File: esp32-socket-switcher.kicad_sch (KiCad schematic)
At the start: 19 parts, among them J1 USB4110GFA, K1 G5CA-1A DC5, Q3 CSD17575Q3T

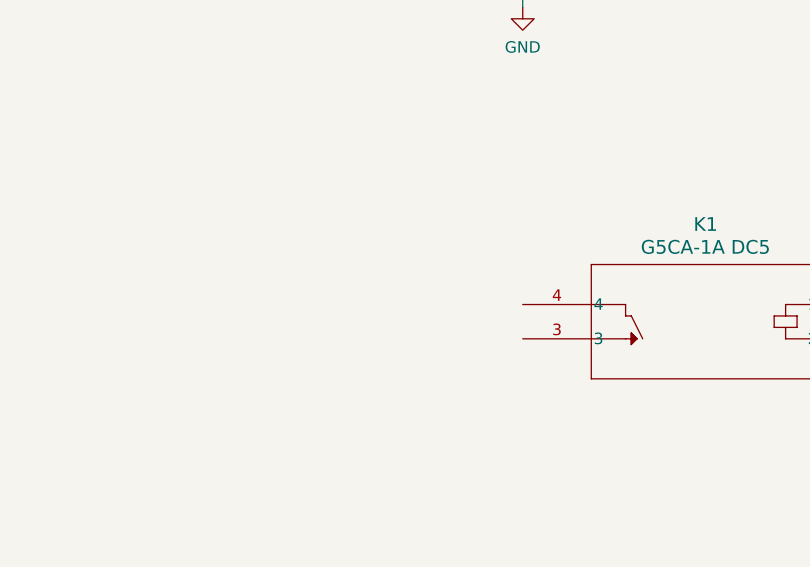
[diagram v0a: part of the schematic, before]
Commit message: mains to relay lable
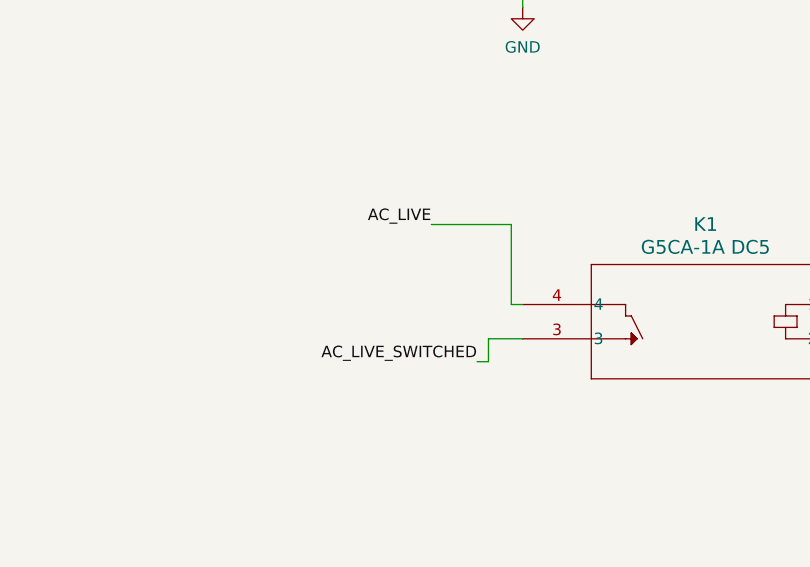
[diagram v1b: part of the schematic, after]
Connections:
- net AC_LIVE: now also K1.4
- net AC_LIVE_SWITCHED: now reaches K1.3
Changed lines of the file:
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@@
+    (stroke (width 0) (type default))
+  )
+  (wire (pts (xy 88.9 95.25) (xy 88.9 92.71))
     (stroke (width 0) (type default))
   )
@@
     (stroke (width 0) (type default))
   )
+  (wire (pts (xy 91.44 88.9) (xy 92.71 88.9))
+    (stroke (width 0) (type default))
+  )
   (wire (pts (xy 33.02 155.575) (xy 35.56 155.575))
     (stroke (width 0) (type default))
   )
+  (wire (pts (xy 91.44 80.01) (xy 91.44 88.9))
+    (stroke (width 0) (type default))
+  )
   (wire (pts (xy 23.495 191.135) (xy 28.575 191.135))
     (stroke (width 0) (type default))
@@
     (stroke (width 0) (type default))
   )
+  (wire (pts (xy 87.63 95.25) (xy 88.9 95.25))
+    (stroke (width 0) (type default))
+  )
   (wire (pts (xy 137.795 180.34) (xy 137.795 173.355))
     (stroke (width 0) (type default))
@@
     (stroke (width 0) (type default))
   )
+  (wire (pts (xy 82.55 80.01) (xy 91.44 80.01))
+    (stroke (width 0) (type default))
+  )
   (wire (pts (xy 92.71 45.72) (xy 92.71 44.45))
     (stroke (width 0) (type default))
@@
     (stroke (width 0) (type default))
   )
+  (wire (pts (xy 88.9 92.71) (xy 92.71 92.71))
+    (stroke (width 0) (type default))
+  )
   (wire (pts (xy 68.58 54.61) (xy 92.71 54.61))
     (stroke (width 0) (type default))
@@
     (effects (font (size 1.27 1.27)) (justify right bottom))
   )
+  (label "AC_LIVE" (at 82.55 80.01 180) (fields_autoplaced)
+    (effects (font (size 1.27 1.27)) (justify right bottom))
+  )
   (label "3V3" (at 156.845 173.355 0) (fields_autoplaced)
     (effects (font (size 1.27 1.27)) (justify left bottom))
@@
     (effects (font (size 1.27 1.27)) (justify left bottom))
   )
+  (label "AC_LIVE_SWITCHED" (at 87.63 95.25 180) (fields_autoplaced)
+    (effects (font (size 1.27 1.27)) (justify right bottom))
+  )
   (label "D-" (at 227.33 111.76 0) (fields_autoplaced)

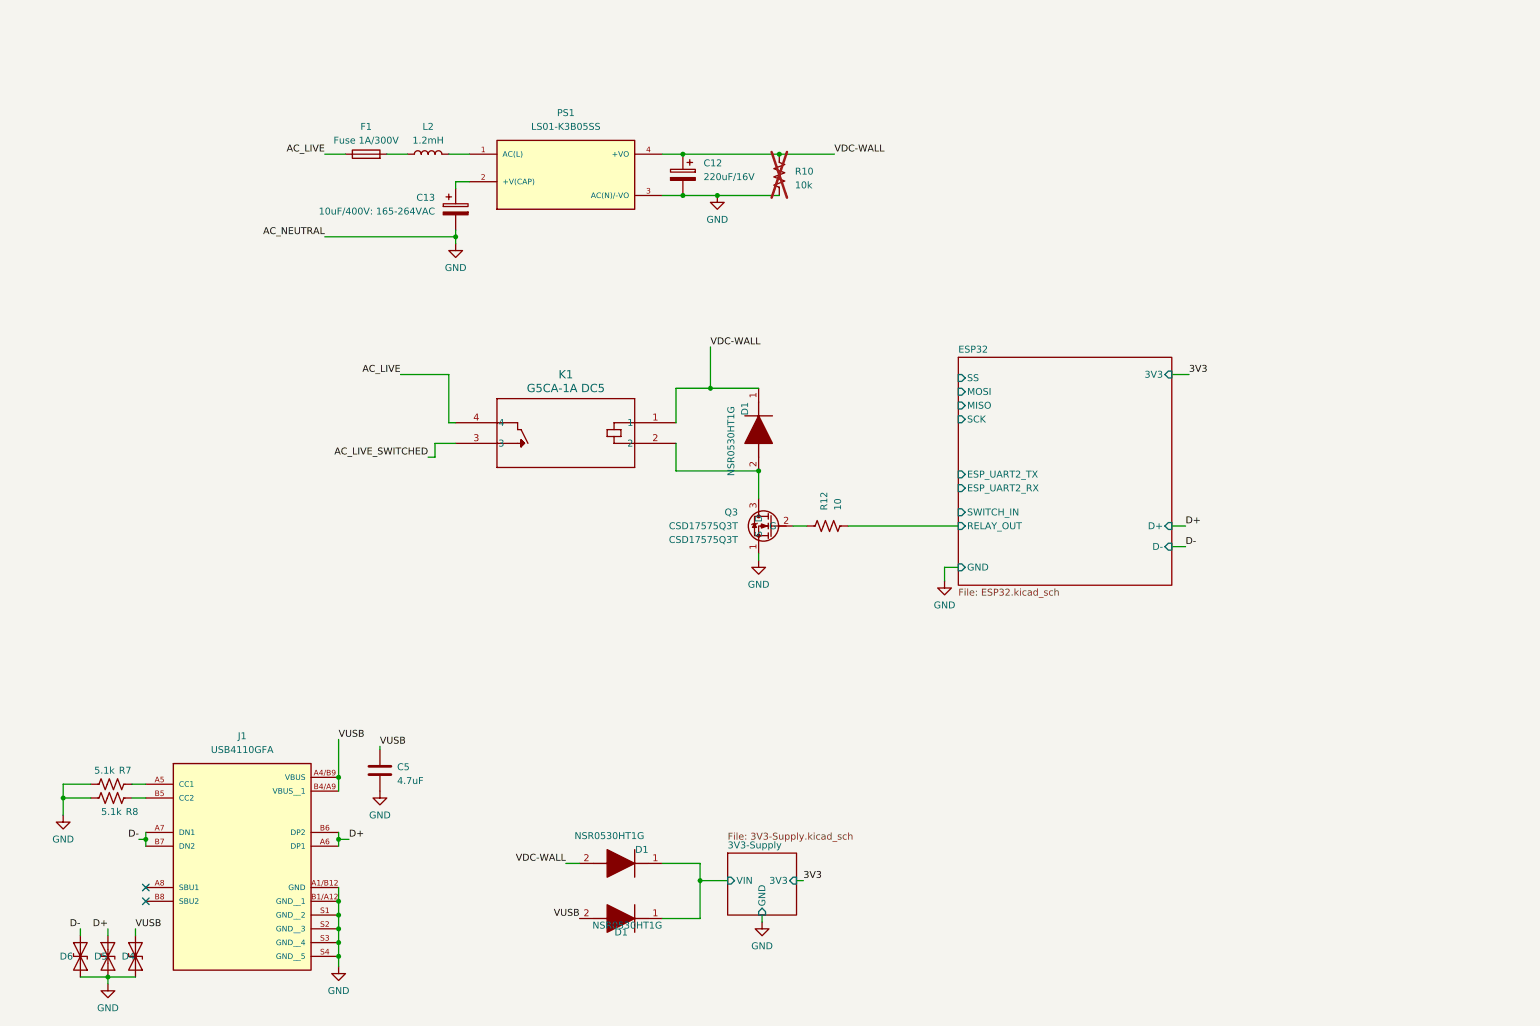
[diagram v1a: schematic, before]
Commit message: added symbols for screw terminals
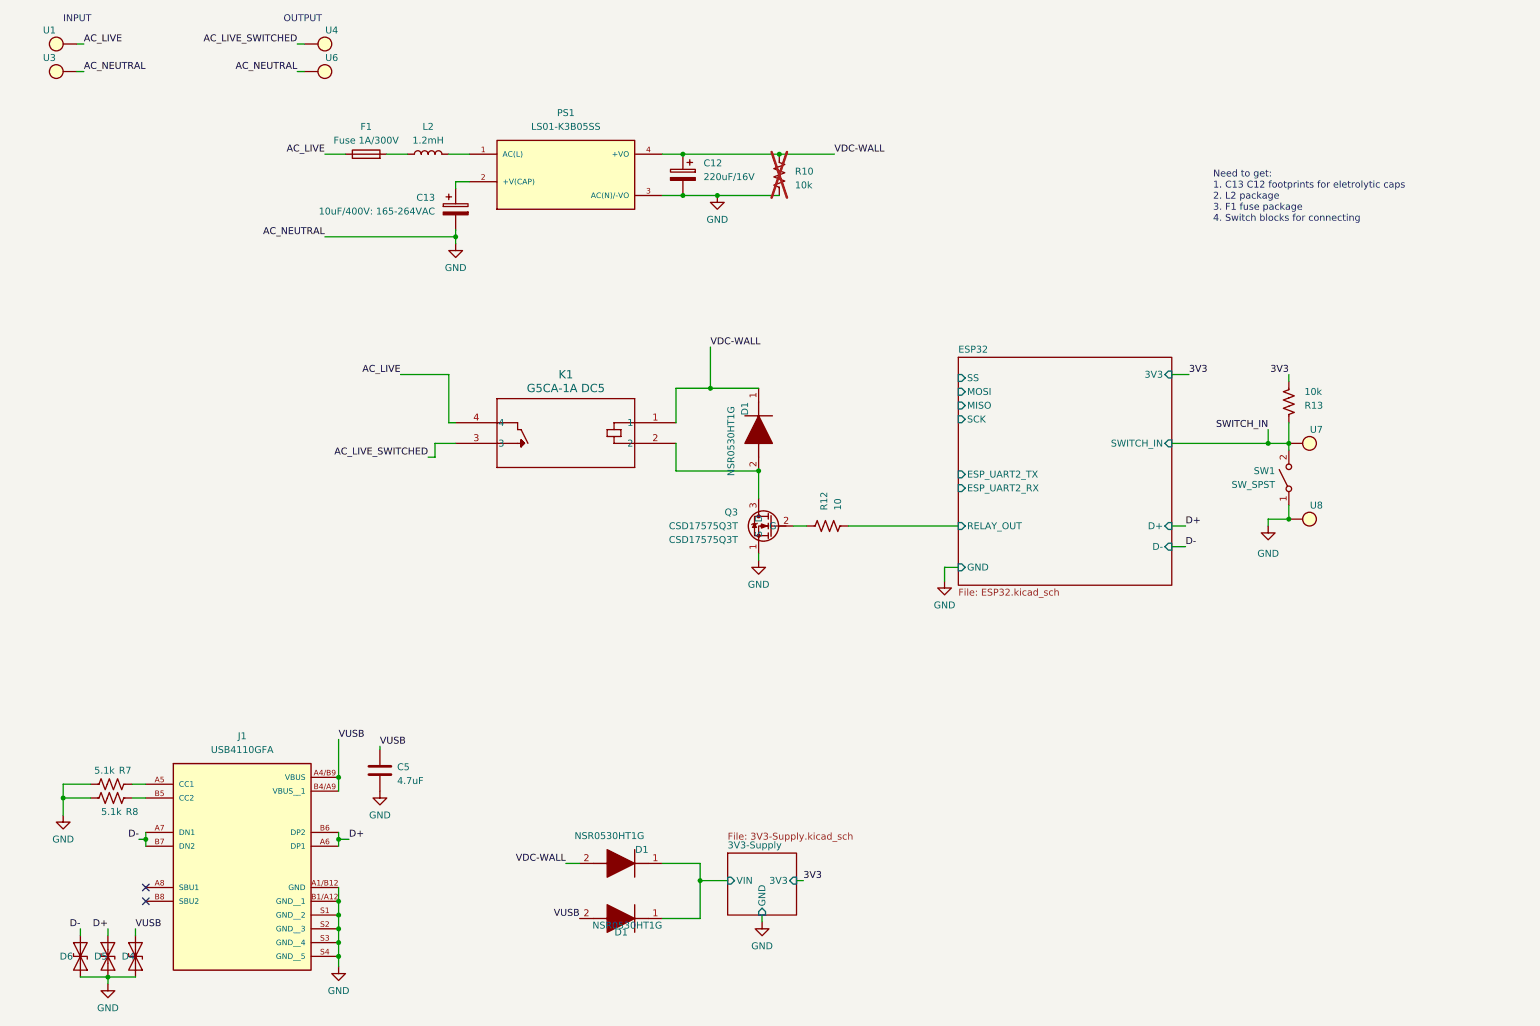
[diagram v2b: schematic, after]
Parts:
- added R13: 10k, esp32-socket-switcher:R_0402_1005Metric, symbol esp32-socket-switcher:Resistor
- added SW1: SW_SPST, symbol Switch:SW_SPST
- added U1, U3, U4, U6, U7, U8: ~, symbol esp32-socket-switcher:PAD_SINGLE
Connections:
- net 3V3: now also R13.1
- net AC_LIVE: now also U1.
- net AC_LIVE_SWITCHED: now also U4.
- net GND: now also SW1.1 (A), U3., U6., U8.
- new net SWITCH_IN: R13.2, SW1.2 (B), U7.
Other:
- note added: "INPUT"
- note added: "Need to get: 1. C13 C12 footprints for eletrolytic caps 2. L2 package 3. F1 fuse package 4. Switch blocks for connecting"
- note added: "OUTPUT"

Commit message: added screw terms. think i need a barrier block instead...
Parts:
- U1, U3, U4, U6, U7, U8: footprint (none) -> esp32-socket-switcher:KEYSTONE_7770
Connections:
- net AC_LIVE: now also U1.1; no longer U1.
- net AC_LIVE_SWITCHED: now also U4.1; no longer U4.
- net GND: now also U3.1, U6.1, U8.1; no longer U3., U6., U8.
- net SWITCH_IN: now also U7.1; no longer U7.
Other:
- note added: "Need to get: 1. C13 C12 footprints for eletrolytic caps 2. L2 package 3. F1 fuse package 4. Replace screw terminals with barrier block(s)"
- note removed: "Need to get: 1. C13 C12 footprints for eletrolytic caps 2. L2 package 3. F1 fuse package 4. Switch blocks for connecting"
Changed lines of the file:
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@@
     (effects (font (size 1.27 1.27)) (justify left bottom))
   )
-  (text "Need to get:\n1. C13 C12 footprints for eletrolytic caps\n2. L2 package\n3. F1 fuse package\n4. Switch blocks for connecting"
+  (text "Need to get:\n1. C13 C12 footprints for eletrolytic caps\n2. L2 package\n3. F1 fuse package\n4. Replace screw terminals with barrier block(s)"
     (at 232.41 52.07 0)
     (effects (font (size 1.27 1.27)) (justify left bottom))
@@
       (effects (font (size 1.27 1.27)))
     )
-    (property "Footprint" "" (at 67.31 19.05 0)
+    (property "Footprint" "esp32-socket-switcher:KEYSTONE_7770" (at 67.31 19.05 0)
       (effects (font (size 1.27 1.27)) hide)
     )
@@
       (effects (font (size 1.27 1.27)) hide)
     )
-    (pin "")
+    (pin "1")
     (instances
       (project "esp32-socket-switcher"
@@
       (effects (font (size 1.27 1.27)))
     )
-    (property "Footprint" "" (at 20.32 19.05 0)
+    (property "Footprint" "esp32-socket-switcher:KEYSTONE_7770" (at 20.32 19.05 0)
       (effects (font (size 1.27 1.27)) hide)
     )
@@
       (effects (font (size 1.27 1.27)) hide)
     )
-    (pin "")
+    (pin "1")
     (instances
       (project "esp32-socket-switcher"
@@
       (effects (font (size 1.27 1.27)))
     )
-    (property "Footprint" "" (at 20.32 24.13 0)
+    (property "Footprint" "esp32-socket-switcher:KEYSTONE_7770" (at 20.32 24.13 0)
       (effects (font (size 1.27 1.27)) hide)
     )
@@
       (effects (font (size 1.27 1.27)) hide)
     )
-    (pin "")
+    (pin "1")
     (instances
       (project "esp32-socket-switcher"
@@
       (effects (font (size 1.27 1.27)))
     )
-    (property "Footprint" "" (at 248.92 92.71 0)
+    (property "Footprint" "esp32-socket-switcher:KEYSTONE_7770" (at 248.92 92.71 0)
       (effects (font (size 1.27 1.27)) hide)
     )
@@
       (effects (font (size 1.27 1.27)) hide)
     )
-    (pin "")
+    (pin "1")
     (instances
       (project "esp32-socket-switcher"
@@
       (effects (font (size 1.27 1.27)))
     )
-    (property "Footprint" "" (at 248.92 106.68 0)
+    (property "Footprint" "esp32-socket-switcher:KEYSTONE_7770" (at 248.92 106.68 0)
       (effects (font (size 1.27 1.27)) hide)
     )
@@
       (effects (font (size 1.27 1.27)) hide)
     )
-    (pin "")
+    (pin "1")
     (instances
       (project "esp32-socket-switcher"
@@
       (effects (font (size 1.27 1.27)))
     )
-    (property "Footprint" "" (at 67.31 24.13 0)
+    (property "Footprint" "esp32-socket-switcher:KEYSTONE_7770" (at 67.31 24.13 0)
       (effects (font (size 1.27 1.27)) hide)
     )
@@
       (effects (font (size 1.27 1.27)) hide)
     )
-    (pin "")
-    (instances
-      (project "esp32-socket-switcher"
+    (pin "1")
+    (instances
+      (project "esp32-socket-switcher"

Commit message: swtiched to barrier block
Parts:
- added J2: 4DB-P108-06, esp32-socket-switcher:TE_2-1437667-9, symbol esp32-socket-switcher:4DB-P108-06
- U1, U3, U4, U6, U7, U8: now left out of the parts list
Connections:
- net AC_LIVE: now also U1., J2.5; no longer U1.1
- net AC_LIVE_SWITCHED: now also U4., J2.6; no longer U4.1
- net GND: now also U3., U6., U8., J2.1, J2.2, J2.3; no longer U3.1, U6.1, U8.1
- net SWITCH_IN: now also U7., J2.4; no longer U7.1
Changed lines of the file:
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@@
   (junction (at 134.62 46.99) (diameter 0) (color 0 0 0 0)
   )
+  (junction (at 34.29 50.8) (diameter 0) (color 0 0 0 0)
+  )
   (junction (at 148.59 97.79) (diameter 0) (color 0 0 0 0)
   )
@@
   )
   (junction (at 140.97 46.99) (diameter 0) (color 0 0 0 0)
+  )
+  (junction (at 34.29 48.26) (diameter 0) (color 0 0 0 0)
   )
   (junction (at 20.32 158.115) (diameter 0) (color 0 0 0 0)
@@
     (stroke (width 0) (type default))
   )
+  (wire (pts (xy 34.29 45.72) (xy 34.29 48.26))
+    (stroke (width 0) (type default))
+  )
   (wire (pts (xy 71.12 179.705) (xy 71.12 177.165))
     (stroke (width 0) (type default))
@@
     (stroke (width 0) (type default))
   )
+  (wire (pts (xy 34.29 48.26) (xy 34.29 50.8))
+    (stroke (width 0) (type default))
+  )
+  (wire (pts (xy 31.75 43.18) (xy 34.29 43.18))
+    (stroke (width 0) (type default))
+  )
   (wire (pts (xy 71.12 184.785) (xy 71.12 182.245))
     (stroke (width 0) (type default))
@@
     (stroke (width 0) (type default))
   )
+  (wire (pts (xy 31.75 40.64) (xy 34.29 40.64))
+    (stroke (width 0) (type default))
+  )
   (wire (pts (xy 63.5 19.05) (xy 64.77 19.05))
     (stroke (width 0) (type default))
@@
   )
   (wire (pts (xy 82.55 80.01) (xy 91.44 80.01))
+    (stroke (width 0) (type default))
+  )
+  (wire (pts (xy 34.29 50.8) (xy 34.29 53.34))
+    (stroke (width 0) (type default))
+  )
+  (wire (pts (xy 31.75 38.1) (xy 34.29 38.1))
     (stroke (width 0) (type default))
   )
@@
     (effects (font (size 1.27 1.27)) (justify right bottom))
   )
+  (label "SWITCH_IN" (at 31.75 43.18 180) (fields_autoplaced)
+    (effects (font (size 1.27 1.27)) (justify right bottom))
+  )
   (label "D+" (at 73.025 165.735 0) (fields_autoplaced)
     (effects (font (size 1.27 1.27)) (justify left bottom))
@@
     (effects (font (size 1.27 1.27)) (justify left bottom))
   )
+  (label "AC_LIVE_SWITCHED" (at 31.75 38.1 180) (fields_autoplaced)
+    (effects (font (size 1.27 1.27)) (justify right bottom))
+  )
   (label "AC_NEUTRAL" (at 63.5 24.13 180) (fields_autoplaced)
     (effects (font (size 1.27 1.27)) (justify right bottom))
@@
   )
   (label "VDC-WALL" (at 113.03 170.18 180) (fields_autoplaced)
+    (effects (font (size 1.27 1.27)) (justify right bottom))
+  )
+  (label "AC_LIVE" (at 31.75 40.64 180) (fields_autoplaced)
     (effects (font (size 1.27 1.27)) (justify right bottom))
   )
@@
   )
   (label "AC_LIVE_SWITCHED" (at 87.63 95.25 180) (fields_autoplaced)
+    (effects (font (size 1.27 1.27)) (justify right bottom))
+  )
+  (label "AC_NEUTRAL" (at 34.29 53.34 180) (fields_autoplaced)
     (effects (font (size 1.27 1.27)) (justify right bottom))
   )
@@
     )
   )
+  (symbol (lib_id "esp32-socket-switcher:4DB-P108-06") (at 44.45 43.18 0) (mirror x) (unit 1)
+    (in_bom yes) (on_board yes) (dnp no)
+    (property "Reference" "J2" (at 50.8 45.72 0)
+      (effects (font (size 1.27 1.27)) (justify left))
+    )
+    (property "Value" "4DB-P108-06" (at 50.8 43.18 0)
+      (effects (font (size 1.27 1.27)) (justify left))
+    )
+    (property "Footprint" "esp32-socket-switcher:TE_2-1437667-9" (at 44.45 43.18 0)
+      (effects (font (size 1.27 1.27)) (justify bottom) hide)
+    )
+    (property "Datasheet" "" (at 44.45 43.18 0)
+      (effects (font (size 1.27 1.27)) hide)
+    )
+    (property "PARTREV" "R" (at 44.45 43.18 0)
+      (effects (font (size 1.27 1.27)) (justify bottom) hide)
+    )
+    (property "STANDARD" "Manufacturer Recommendations" (at 44.45 43.18 0)
+      (effects (font (size 1.27 1.27)) (justify bottom) hide)
+    )
+    (property "MANUFACTURER" "TE" (at 44.45 43.18 0)
+      (effects (font (size 1.27 1.27)) (justify bottom) hide)
+    )
+    (pin "1")
+    (pin "2")
+    (pin "3")
+    (pin "4")
+    (pin "5")
+    (pin "6")
+    (instances
+      (project "esp32-socket-switcher"
+        (path "/19e4cb9f-d0a4-4ce0-8aa4-5fe95563dc37"
+          (reference "J2") (unit 1)
+        )
+      )
+    )
+  )
   (symbol (lib_id "esp32-socket-switcher:PAD_SINGLE") (at 67.31 19.05 0) (mirror y) (unit 1)
-    (in_bom yes) (on_board yes) (dnp no)
+    (in_bom no) (on_board no) (dnp no)
     (property "Reference" "U4" (at 69.85 16.51 0)
       (effects (font (size 1.27 1.27)))
@@
       (effects (font (size 1.27 1.27)) hide)
     )
-    (pin "1")
+    (pin "")
     (instances
       (project "esp32-socket-switcher"
@@
   )
   (symbol (lib_id "esp32-socket-switcher:PAD_SINGLE") (at 20.32 19.05 0) (unit 1)
-    (in_bom yes) (on_board yes) (dnp no)
+    (in_bom no) (on_board no) (dnp no)
     (property "Reference" "U1" (at 17.78 16.51 0)
       (effects (font (size 1.27 1.27)))
@@
       (effects (font (size 1.27 1.27)) hide)
     )
-    (pin "1")
+    (pin "")
     (instances
       (project "esp32-socket-switcher"
@@
   )
   (symbol (lib_id "esp32-socket-switcher:PAD_SINGLE") (at 20.32 24.13 0) (unit 1)
-    (in_bom yes) (on_board yes) (dnp no)
+    (in_bom no) (on_board no) (dnp no)
     (property "Reference" "U3" (at 17.78 21.59 0)
       (effects (font (size 1.27 1.27)))
@@
       (effects (font (size 1.27 1.27)) hide)
     )
-    (pin "1")
+    (pin "")
     (instances
       (project "esp32-socket-switcher"
@@
   )
   (symbol (lib_id "esp32-socket-switcher:PAD_SINGLE") (at 248.92 92.71 0) (mirror y) (unit 1)
-    (in_bom yes) (on_board yes) (dnp no)
+    (in_bom no) (on_board no) (dnp no)
     (property "Reference" "U7" (at 251.46 90.17 0)
       (effects (font (size 1.27 1.27)))
@@
       (effects (font (size 1.27 1.27)) hide)
     )
-    (pin "1")
+    (pin "")
     (instances
       (project "esp32-socket-switcher"
@@
   )
   (symbol (lib_id "esp32-socket-switcher:PAD_SINGLE") (at 248.92 106.68 0) (mirror y) (unit 1)
-    (in_bom yes) (on_board yes) (dnp no)
+    (in_bom no) (on_board no) (dnp no)
     (property "Reference" "U8" (at 251.46 104.14 0)
       (effects (font (size 1.27 1.27)))
@@
       (effects (font (size 1.27 1.27)) hide)
     )
-    (pin "1")
+    (pin "")
     (instances
       (project "esp32-socket-switcher"
@@
   )
   (symbol (lib_id "esp32-socket-switcher:PAD_SINGLE") (at 67.31 24.13 0) (mirror y) (unit 1)
-    (in_bom yes) (on_board yes) (dnp no)
+    (in_bom no) (on_board no) (dnp no)
     (property "Reference" "U6" (at 69.85 21.59 0)
       (effects (font (size 1.27 1.27)))
@@
       (effects (font (size 1.27 1.27)) hide)
     )
-    (pin "1")
-    (instances
-      (project "esp32-socket-switcher"
+    (pin "")
+    (instances
+      (project "esp32-socket-switcher"

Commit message: added caps and placed them
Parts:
- removed R8: 5.1k, esp32-socket-switcher:R_0402_1005Metric, symbol NeuralStimulatorAndRecorder:Resistor
- C12: footprint (none) -> esp32-socket-switcher:CAP_EEEFK1C221XP; symbol Device:C_Polarized -> esp32-socket-switcher:EEE-FK1C221XP
- C13: footprint (none) -> esp32-socket-switcher:U1-S_NCH; symbol Device:C_Polarized -> esp32-socket-switcher:UCY2G100MPD
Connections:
- net at J1.B5 (CC2): now also J1.A5 (CC1), R7.2
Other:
- sheet ESP32 ports: added VUSB; removed none
- moved on the sheet: C5, D4, D5, D6, J1, R7
